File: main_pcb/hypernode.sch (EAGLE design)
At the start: 133 parts, among them IC1 74HCT245D, J1 AVR_SPI_PRG_62X3_LOCK, U1 MAX488, U2 PCA9685, U3 VOLTAGE_REGULATORDPACK, U4 ATMEGA328P, U5 MAX3421E, X1 USB-A-H, X10 JST-XH-03-PIN-LONG-PAD, X2 JST-XH-CONNECTOR-02-PIN, X4 JST-XH-CONNECTOR-02-PIN, X7 JST-XH-03-PIN-LONG-PAD, X8 JST-XH-03-PIN-LONG-PAD, X9 JST-XH-03-PIN-LONG-PAD, Y1 8MHZ

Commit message: remove unnecessary components from main pcb
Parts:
- removed C2, C3, C4, C6, C7: 100nF, Multischriever:CAPACITOR_0603
- removed C8: 1uF, Multischriever:CAPACITOR_0603
- removed C9: 4.7uF, Multischriever:CAPACITOR_0603
- removed D1, D3: (no value), Multischriever:DIODE_SOD-523
- removed HCPL0453: HCPL0700, optocoupler:HCPL0452
- removed J1: AVR_SPI_PRG_62X3_LOCK, SparkFun-Connectors:AVR_SPI_PRG_62X3_LOCK
- removed LED11, LED13, LED14, LED15, LED16, LED17, LED18, LED2, LED3, LED5, LED7, LED9: (no value), Multischriever:LED0603
- removed R12, R15, R18, R19, R22, R23, R26, R27, R3, R30, R31, R32, R33, R34, R35, R36, R37, R38, R39, R40, R41, R5: (no value), Multischriever:RESISTOR
- removed R13, R45, R46, R47: 180R, Multischriever:RESISTOR
- removed R14: 1K, Multischriever:RESISTOR
- removed R21, R24: 1k, Multischriever:RESISTOR
- removed R25, R28, R29, R42: 10k, Multischriever:RESISTOR
- removed R43, R44, R57: 4k7, Multischriever:RESISTOR
- removed R48, R50, R55, R56: 10K, Multischriever:RESISTOR
- removed R49, R9: 470R, Multischriever:RESISTOR
- removed R52: 100R, Multischriever:RESISTOR
- removed R53, R54, R6, R7: 33R, Multischriever:RESISTOR
- removed R8: 220R, Multischriever:RESISTOR
- removed REMOTE: M05X2NO_SILK, SparkFun-Connectors:M05X2NO_SILK
- removed U$1: ESP32POE, Multischriever:ESP32POE
- removed U$10, U$12, U$14, U$16, U$18, U$19, U$20, U$21, U$22, U$23, U$5, U$7: NCV8401_LOAD_SWITCH'DPAK+SOT23', Multischriever:NCV8401_LOAD_SWITCH'DPAK+SOT23'
- removed U$2, U$6: BIGTERMINAL, Multischriever:BIGTERMINAL
- removed U$24: 12MHz, adafruit:CERMOSCILL-AWCSR
- removed U$9: ESP8266_ESP12NOSILK, Multischriever:ESP8266_ESP12NOSILK
- removed U2: PCA9685, SparkFun-DigitalIC:PCA9685
- removed U3: VOLTAGE_REGULATORDPACK, Multischriever:VOLTAGE_REGULATORDPACK
- removed U4: ATMEGA328P, SparkFun-DigitalIC:ATMEGA328_SMT
- removed U5: MAX3421E, SparkFun-DigitalIC:MAX3421ESMD
- removed X1: USB-A-H, con-usb:USB-A-H
- removed X10, X9: JST-XH-03-PIN-LONG-PAD, Rembrandt Electronics - JST XH Connectors v1-0:JST-XH-03-PIN-LONG-PAD
- removed X11, X14, X16, X17, X19, X21, X22, X23, X24, X25, X26, X3: (no value), Multischriever:SCREW_TERMINAL_02-PINGREEN
- removed Y1: 8MHZ, SparkFun-FreqCtrl:RESONATOR8MHZ
- added U$17: WT32-ETH01, Multischriever:WT32-ETH01
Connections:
- removed net ENCA: R48.2, REMOTE.8, U$1.GPI34_BUT1
- removed net ENCBTN: R49.2, REMOTE.4, U$1.GPI39
- removed net MIDIIN: R50.2, R52.2, REMOTE.6, U$1.GPI35
- removed net N$1: R45.1, REMOTE.3
- removed net N$11: R45.2, U2.CH13
- removed net N$12: R46.1, REMOTE.5
- removed net N$14: R6.1, X10-1.S
- removed net N$15: R7.1, X10-3.S
- removed net N$17: D1.A, HCPL0453.C, X9-3.S
- removed net N$19: R5.1, U$7.G
- removed net N$20: R8.1, X9-1.S
- removed net N$21: D1.C, HCPL0453.A, R8.2
- removed net N$22: LED2.A, R3.1
- removed net N$23: R29.1, U$9.REST
- removed net N$24: LED2.C, U$7.D, X3-2.KL
- removed net N$27: R42.1, U$9.CH_PD
- removed net N$29: R21.2, U$9.TXD
- removed net N$30: R24.2, U$9.RXD
- removed net N$31: R28.2, U$9.GPIO0
- removed net N$32: R25.2, U$9.GPIO15
- removed net N$33: R47.1, REMOTE.7
- removed net N$35: R15.1, U$10.G
- removed net N$36: LED5.A, R12.1
- removed net N$37: LED5.C, U$10.D, X11-2.KL
- removed net N$39: HCPL0453.VO, R52.1, R9.2
- removed net N$40: U4.PB6(XTAL1/TOSC1), Y1.1
- removed net N$41: U4.PB7(XTAL2/TOSC2), Y1.3
- removed net N$42: U4.PD5(T1), U5.RES
- removed net N$43: R54.1, X1.D+
- removed net N$44: R53.1, X1.D-
- removed net N$45: LED3.C, U$5.D, X17-2.KL
- removed net N$46: R14.1, U$5.G
- removed net N$47: R19.1, U$12.G
- removed net N$48: LED7.A, R18.1
- removed net N$49: LED7.C, U$12.D, X14-2.KL
- removed net N$50: R53.2, U5.D-
- removed net N$51: R54.2, U5.D+
- removed net N$52: U$24.OUT, U5.X1
- removed net N$53: U$24.IN, U5.X0
- removed net N$54: U4.PD2(INT0), U5.INT
- removed net N$55: U4.PD3(INT1), U5.GPX
- removed net N$56: J1.4, U4.PB3(MOSI/OC2), U5.MOSI
- removed net N$57: J1.1, U4.PB4(MISO), U5.MISO
- removed net N$58: J1.3, U4.PB5(SCK), U5.SCK
- removed net N$59: R23.1, U$14.G
- removed net N$60: LED9.A, R22.1
- removed net N$61: LED9.C, U$14.D, X16-2.KL
- removed net N$62: LED3.A, R13.1
- removed net N$63: R56.1, U4.PB2(SS/OC1B), U5.SS
- removed net N$64: J1.5, R55.1, U4.PC6(/RESET)
- removed net N$68: D3.C, U4.PD1(TXD)
- removed net N$7: R47.2, U2.CH15
- removed net N$71: R27.1, U$16.G
- removed net N$72: LED11.A, R26.1
- removed net N$73: LED11.C, U$16.D, X19-2.KL
- removed net N$77: R31.1, U$18.G
- removed net N$78: LED13.A, R30.1
- removed net N$79: LED13.C, U$18.D, X21-2.KL
- removed net N$80: R33.1, U$19.G
- removed net N$81: LED14.A, R32.1
- removed net N$82: LED14.C, U$19.D, X22-2.KL
- removed net N$83: R35.1, U$20.G
- removed net N$84: LED15.A, R34.1
- removed net N$85: LED15.C, U$20.D, X23-2.KL
- removed net N$86: R37.1, U$21.G
- removed net N$87: LED16.A, R36.1
- removed net N$88: LED16.C, U$21.D, X24-2.KL
- removed net N$89: R39.1, U$22.G
- removed net N$9: R46.2, U2.CH14
- removed net N$90: LED17.A, R38.1
- removed net N$91: LED17.C, U$22.D, X25-2.KL
- removed net N$92: R41.1, U$23.G
- removed net N$93: LED18.A, R40.1
- removed net N$94: LED18.C, U$23.D, X26-2.KL
- removed net SCL: R44.1, REMOTE.10, U$1.GPIO16_I2C_SCL, U$9.GPIO5, U2.SCL, U4.PC5(ADC5/SCL)
- removed net SDA: R43.1, REMOTE.9, U$1.GPIO13_I2C_SDA, U$9.GPIO4, U2.SDA, U4.PC4(ADC4/SDA)
- removed net T1DRIVE1: R13.2, R14.2, U2.CH8
- removed net T1DRIVE10: R34.2, R35.2, U2.CH7
- removed net T1DRIVE11: R32.2, R33.2, U2.CH6
- removed net T1DRIVE12: R30.2, R31.2, U2.CH2
- removed net T1DRIVE2: R3.2, R5.2, U2.CH9
- removed net T1DRIVE3: R12.2, R15.2, U2.CH10
- removed net T1DRIVE4: R18.2, R19.2, U2.CH11
- removed net T1DRIVE5: R22.2, R23.2, U2.CH1
- removed net T1DRIVE6: R26.2, R27.2, U2.CH0
- removed net T1DRIVE7: R40.2, R41.2, U2.CH5
- removed net T1DRIVE8: R38.2, R39.2, U2.CH4
- removed net T1DRIVE9: R36.2, R37.2, U2.CH3
- removed net USBRX: D3.A, R57.2, U$1.GPIO3_U0RXD
- removed net USBTX: U$1.GPIO1_U0TXD, U4.PD0(RXD)
- new net DMXOUT: U$17.TXD, U1.DI
- net +3V3: now also U$17.3V3, U$17.3V3@1; no longer C2.1, C3.1, C4.1, C6.1, C7.1, C8.1, HCPL0453.VCC, J1.2, R28.1, R29.2, R42.2, R43.2, R44.2, R48.1, R50.1, R55.2, R56.2, R57.1, R6.2, R9.1, REMOTE.1, U$1.3V3, U$9.VCC, U2.VDD, U3.OUT, U4.AREF, U4.AVCC, U4.VCC@1, U4.VCC@2, U5.VCC, U5.VL
- net +5V: now also U$17.5V; no longer C9.1, U$1.5V, U3.IN, X1.VBUS
- net DMXIN: now also U$17.IO36; no longer R24.1, U$1.GPI36_U1RXD
- net GND: now also U$17.GND, U$17.GND@1, U$17.GND@2, U$17.GND@3, U$17.GND@4; no longer C2.2, C3.2, C4.2, C6.2, C7.2, C8.2, C9.2, HCPL0453.GND, J1.6, R25.1, R49.1, REMOTE.2, U$1.GND, U$10.S, U$12.S, U$14.S, U$16.S, U$18.S, U$19.S, U$2.P$1, U$20.S, U$21.S, U$22.S, U$23.S, U$24.GND, U$5.S, U$6.P$2, U$7.S, U$9.GND, U2.!OE, U2.A0, U2.A1, U2.A2, U2.A3, U2.A4, U2.A5, U2.EXTCLK, U2.VSS, U3.ADJ, U4.AGND, U4.GND@1, U4.GND@2, U5.GND@19, U5.GND@3, X1.GND, X10-2.S, Y1.2
- net VDD: no longer U$2.P$2, U$6.P$1, X11-1.KL, X14-1.KL, X16-1.KL, X17-1.KL, X19-1.KL, X21-1.KL, X22-1.KL, X23-1.KL, X24-1.KL, X25-1.KL, X26-1.KL, X3-1.KL
- net WS1: now also U$17.RXD; no longer R7.2, U$1.GPIO5_SPI_CS, U$9.GPIO16
- net WS2: now also U$17.IO4; no longer U$1.GPIO4_U1TXD, U$9.GPIO14
- net WS3: now also U$17.IO14; no longer U$1.GPIO14_HS2_CLK
- net WS4: now also U$17.IO2; no longer U$1.GPIO2_HS2_DATA0, U$9.GPIO12
- net WS5: now also U$17.IO15; no longer U$1.GPIO15_HS2_CMD
- net WS6: now also U$17.CFG; no longer R21.1, U$1.GPIO32, U1.DI
- net WS7: now also U$17.IO0; no longer U$1.GPIO0, U$9.GPIO13
- net WS8: now also U$17.485_EN; no longer U$1.GPIO33
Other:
- note removed: "BOOTPWM"
- note removed: "BOOTPWM, PU"
- note removed: "IN"
- note removed: "IN, BTN"
- note removed: "IN, DMX"
- note removed: "IN, MIDI"
- note removed: "SD"
- note removed: "SD, PD"
- note removed: "USBRX"
- note removed: "USBTX"
- note removed: "extra protection for if someone screws up the rotary encoder connections and connects 3v3 to this line"

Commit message: further cleanup and arrangement
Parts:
- removed R10: 100R, Multischriever:RESISTOR
- added C2: 100nF, Multischriever:CAPACITOR_0603
- added LED2: (no value), Multischriever:LED0603
- added PROGRAM: (no value), pinhead:PINHD-1X6
- added R3: 100R, Multischriever:RESISTOR
- added R5: 180R, Multischriever:RESISTOR
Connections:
- removed net N$10: IC1A.B6, R16.1
- removed net N$18: R20.2, U$11.6
- removed net N$25: R16.2, U$11.4
- removed net N$26: R10.2, U$11.2
- removed net N$28: R4.2, U$13.6
- removed net N$3: IC1A.B1, R1.1
- removed net N$5: IC1A.B2, R2.1
- removed net N$6: IC1A.B3, R4.1
- removed net N$8: IC1A.B5, R10.1
- removed net NIKS: IC1A.B4, R11.1
- removed net WS1-2: R1.2, U$13.2
- removed net WS2-2: R2.2, U$13.4
- removed net WS4-2: R11.2, U$13.8
- new net N$1: LED2.A, R5.1
- new net N$11: IC1A.B2, R20.1
- new net N$12: IC1A.B3, R16.1
- new net N$14: IC1A.B5, R11.1
- new net N$15: IC1A.B6, R4.1
- new net N$17: IC1A.B8, R1.1
- new net N$9: IC1A.B1, R17.1
- net +5V: now also C2.1
- net GND: now also C2.2, LED2.C
- net N$13: now also IC1A.B4, R3.1; no longer IC1A.B7, R20.1
- net N$16: now also IC1A.B7, R2.1; no longer IC1A.B8, R17.1
- net N$2: now also R5.2, U$17.IO12; no longer R17.2, U$11.8
- net WS1: now also IC1A.A4; no longer IC1A.A1
- net WS2: now also IC1A.A3; no longer IC1A.A2
- net WS3: now also IC1A.A2; no longer IC1A.A3
- net WS4: now also IC1A.A1; no longer IC1A.A4
- net WS5: now also IC1A.A8; no longer IC1A.A5
- net WS6: now also IC1A.A7; no longer IC1A.A6
- net WS7: now also IC1A.A6; no longer IC1A.A7
- net WS8: now also IC1A.A5; no longer IC1A.A8
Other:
- moved on the sheet: C5, IC1P, R1, R11, R16, R17, R2, R20, R4, U$11, U$13

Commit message: programmer
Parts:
- removed LED2: (no value), Multischriever:LED0603
- added LED_STATUS: (no value), Multischriever:LED0603
- added R7: 10K, Multischriever:RESISTOR
- U$17: value WT32-ETH01 -> WT32-ETH01WT32-ETH01-SMD; device Multischriever:WT32-ETH01 -> Multischriever:WT32-ETH01WT32-ETH01-SMD
- renumbered LED1 to LED_PWR
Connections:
- removed net N$2: R5.2, U$17.IO12
- new net EN: PROGRAM.4, U$17.EN, U$17.EN@1
- new net N$10: R2.2, U$13.4
- new net N$18: R4.2, U$13.6
- new net N$19: R11.2, U$13.8
- new net N$3: R3.2, U$11.2
- new net N$5: R16.2, U$11.4
- new net N$6: R20.2, U$11.6
- new net N$7: R17.2, U$11.8
- new net N$8: R1.2, U$13.2
- new net RX: PROGRAM.3, U$17.RX0
- new net TX: PROGRAM.2, U$17.TX0
- net +3V3: now also PROGRAM.1
- net DMXOUT: now also R5.1
- net GND: now also LED_STATUS.C, PROGRAM.6, R7.2; no longer LED2.C
- net N$1: now also LED_STATUS.A, R5.2; no longer LED2.A, R5.1
- net WS4: now also R7.1
- net WS7: now also PROGRAM.5, U$17.IO12; no longer U$17.IO0
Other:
- moved on the sheet: R5

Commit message: routing
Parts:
- removed U$8: POWERPOLE, Multischriever:POWERPOLE
- added R6: 180R, Multischriever:RESISTOR
- R5: value 180R -> 1K
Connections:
- new net N$2: LED_STATUS.A, R6.1
- new net N$20: U$17.3V3@1
- net +3V3: no longer U$17.3V3@1
- net DMXOUT: no longer R5.1
- net EN: no longer U$17.EN@1
- net GND: no longer U$8.P$2
- net N$1: now also PROGRAM.3, R5.1; no longer LED_STATUS.A, R5.2
- net RX: now also R5.2, R6.2; no longer PROGRAM.3
- net VDD: no longer U$8.P$1
- net WS1: now also U$17.IO14; no longer U$17.RXD
- net WS2: now also U$17.IO12; no longer U$17.IO4
- net WS3: now also U$17.IO4; no longer U$17.IO14
- net WS4: now also PROGRAM.5
- net WS6: now also U$17.RXD; no longer U$17.CFG
- net WS7: now also U$17.485_EN; no longer PROGRAM.5, U$17.IO12
- net WS8: now also U$17.CFG; no longer U$17.485_EN
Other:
- note added: "Do not use IO0. (RMII Clk)"
- moved on the sheet: LED_STATUS, R5

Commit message: rev A
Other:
- note added: "Input only"
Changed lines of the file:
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@@
 <plain>
 <text x="114.3" y="68.58" size="1.778" layer="91">Do not use IO0. (RMII Clk)</text>
+<text x="114.3" y="63.5" size="1.778" layer="91">Input only</text>
+<text x="114.3" y="50.8" size="1.778" layer="91">Input only</text>
 </plain>
 <instances>

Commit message: fix boot connetion
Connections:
- new net IO0: PROGRAM.5, U$17.IO0
- net WS4: no longer PROGRAM.5
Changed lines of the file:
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@@
 <description>MCU</description>
 <plain>
-<text x="114.3" y="68.58" size="1.778" layer="91">Do not use IO0. (RMII Clk)</text>
+<text x="127" y="68.58" size="1.778" layer="91">Do not use IO0.
+(RMII Clk)</text>
 <text x="114.3" y="63.5" size="1.778" layer="91">Input only</text>
 <text x="114.3" y="50.8" size="1.778" layer="91">Input only</text>
@@
 <label x="152.4" y="71.12" size="1.778" layer="95"/>
 </segment>
-<segment>
-<pinref part="PROGRAM" gate="A" pin="5"/>
-<wire x1="15.24" y1="-2.54" x2="-7.62" y2="-2.54" width="0.1524" layer="91"/>
-<label x="-7.62" y="-2.54" size="1.778" layer="95"/>
-</segment>
 </net>
 <net name="WS5" class="0">
@@
 </segment>
 </net>
+<net name="IO0" class="0">
+<segment>
+<pinref part="U$17" gate="G$1" pin="IO0"/>
+<wire x1="109.22" y1="68.58" x2="124.46" y2="68.58" width="0.1524" layer="91"/>
+<label x="121.92" y="68.58" size="1.778" layer="95"/>
+</segment>
+<segment>
+<pinref part="PROGRAM" gate="A" pin="5"/>
+<wire x1="15.24" y1="-2.54" x2="-7.62" y2="-2.54" width="0.1524" layer="91"/>
+<label x="-7.62" y="-2.54" size="1.778" layer="95"/>
+</segment>
+</net>
 </nets>
 </sheet>
@@
 </drawing>
 <compatibility>
+<note version="6.3" minversion="6.2.2" severity="warning">
+Since Version 6.2.2 text objects can contain more than one line,
+which will not be processed correctly with this version.
+</note>
 <note version="8.2" severity="warning">
 Since Version 8.2, EAGLE supports online libraries. The ids

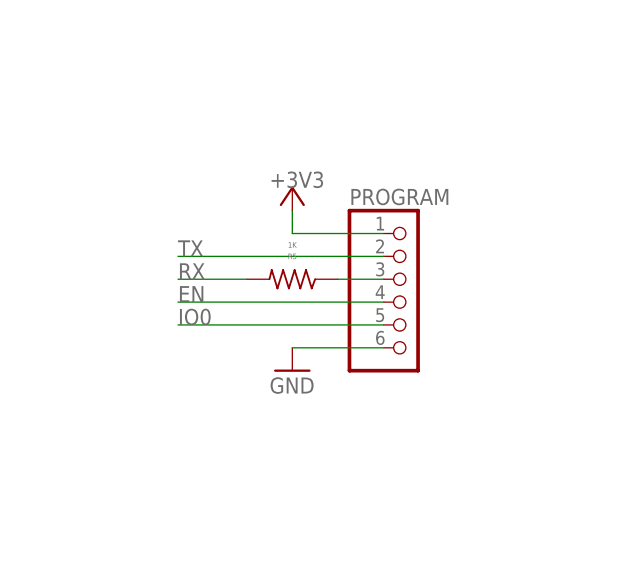
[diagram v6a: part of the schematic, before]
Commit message: change rx resistor to 2x100r
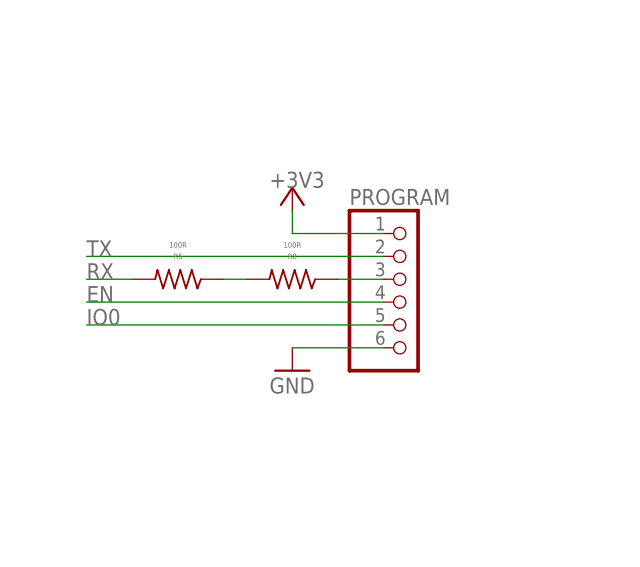
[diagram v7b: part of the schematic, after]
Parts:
- added R8: 100R, Multischriever:RESISTOR
- R5: value 1K -> 100R
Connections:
- new net N$21: PROGRAM.3, R8.1
- net N$1: now also R8.2; no longer PROGRAM.3
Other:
- moved on the sheet: R5
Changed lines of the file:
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@@
 <part name="LED_STATUS" library="Multischriever" deviceset="LED" device="0603"/>
 <part name="GND11" library="supply1" library_urn="urn:adsk.eagle:library:371" deviceset="GND" device=""/>
-<part name="R5" library="Multischriever" deviceset="RESISTOR" device="" value="1K"/>
+<part name="R5" library="Multischriever" deviceset="RESISTOR" device="" value="100R"/>
+<part name="R8" library="Multischriever" deviceset="RESISTOR" device="" value="100R"/>
 </parts>
 <sheets>
@@
 <attribute name="VALUE" x="134.62" y="86.36" size="1.778" layer="96"/>
 </instance>
-<instance part="R5" gate="G$1" x="5.08" y="2.54" smashed="yes" rot="R180">
+<instance part="R5" gate="G$1" x="-7.62" y="2.54" smashed="yes" rot="R180">
+<attribute name="NAME" x="-7.62" y="5.08" size="0.6096" layer="95" rot="R180" align="center"/>
+<attribute name="VALUE" x="-7.62" y="6.35" size="0.6096" layer="96" rot="R180" align="center"/>
+</instance>
+<instance part="R8" gate="G$1" x="5.08" y="2.54" smashed="yes" rot="R180">
 <attribute name="NAME" x="5.08" y="5.08" size="0.6096" layer="95" rot="R180" align="center"/>
 <attribute name="VALUE" x="5.08" y="6.35" size="0.6096" layer="96" rot="R180" align="center"/>
@@
 <segment>
 <pinref part="PROGRAM" gate="A" pin="2"/>
-<wire x1="15.24" y1="5.08" x2="-7.62" y2="5.08" width="0.1524" layer="91"/>
-<label x="-7.62" y="5.08" size="1.778" layer="95"/>
+<wire x1="15.24" y1="5.08" x2="-17.78" y2="5.08" width="0.1524" layer="91"/>
+<label x="-17.78" y="5.08" size="1.778" layer="95"/>
 </segment>
 </net>
@@
 </segment>
 <segment>
-<label x="-7.62" y="2.54" size="1.778" layer="95"/>
+<label x="-17.78" y="2.54" size="1.778" layer="95"/>
 <pinref part="R5" gate="G$1" pin="2"/>
-<wire x1="0" y1="2.54" x2="-7.62" y2="2.54" width="0.1524" layer="91"/>
+<wire x1="-12.7" y1="2.54" x2="-17.78" y2="2.54" width="0.1524" layer="91"/>
 </segment>
 </net>
@@
 <segment>
 <pinref part="PROGRAM" gate="A" pin="4"/>
-<wire x1="15.24" y1="0" x2="-7.62" y2="0" width="0.1524" layer="91"/>
-<label x="-7.62" y="0" size="1.778" layer="95"/>
+<wire x1="15.24" y1="0" x2="-17.78" y2="0" width="0.1524" layer="91"/>
+<label x="-17.78" y="0" size="1.778" layer="95"/>
 </segment>
 </net>
@@
 </segment>
 </net>
-<net name="N$1" class="0">
-<segment>
-<pinref part="R5" gate="G$1" pin="1"/>
-<pinref part="PROGRAM" gate="A" pin="3"/>
-<wire x1="10.16" y1="2.54" x2="15.24" y2="2.54" width="0.1524" layer="91"/>
-</segment>
-</net>
 <net name="N$20" class="0">
 <segment>
@@
 <segment>
 <pinref part="PROGRAM" gate="A" pin="5"/>
-<wire x1="15.24" y1="-2.54" x2="-7.62" y2="-2.54" width="0.1524" layer="91"/>
-<label x="-7.62" y="-2.54" size="1.778" layer="95"/>
-</segment>
-</net>
+<wire x1="15.24" y1="-2.54" x2="-17.78" y2="-2.54" width="0.1524" layer="91"/>
+<label x="-17.78" y="-2.54" size="1.778" layer="95"/>
+</segment>
+</net>
+<net name="N$1" class="0">
+<segment>
+<pinref part="R5" gate="G$1" pin="1"/>
+<pinref part="R8" gate="G$1" pin="2"/>
+<wire x1="-2.54" y1="2.54" x2="0" y2="2.54" width="0.1524" layer="91"/>
+</segment>
+</net>
+<net name="N$21" class="0">
+<segment>
+<pinref part="R8" gate="G$1" pin="1"/>
+<pinref part="PROGRAM" gate="A" pin="3"/>
+<wire x1="10.16" y1="2.54" x2="15.24" y2="2.54" width="0.1524" layer="91"/>
+</segment>
+</net>

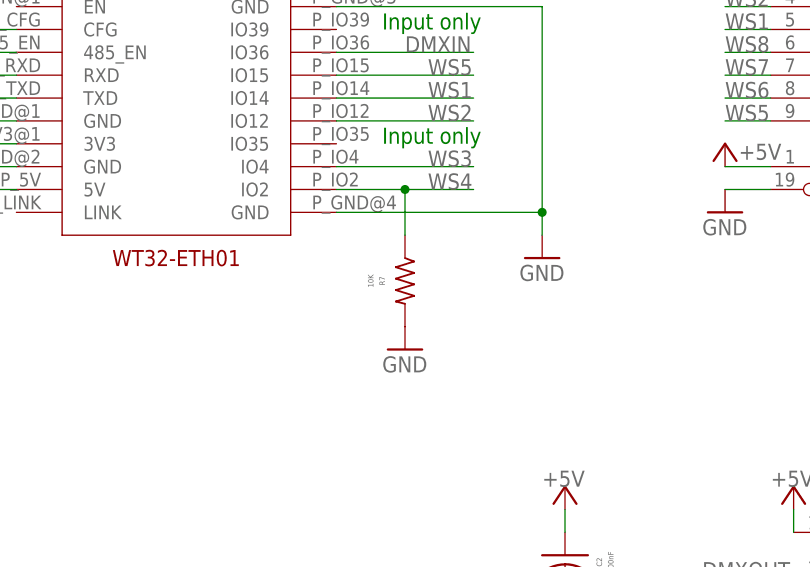
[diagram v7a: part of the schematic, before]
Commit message: remove unnecessary pull down resistor
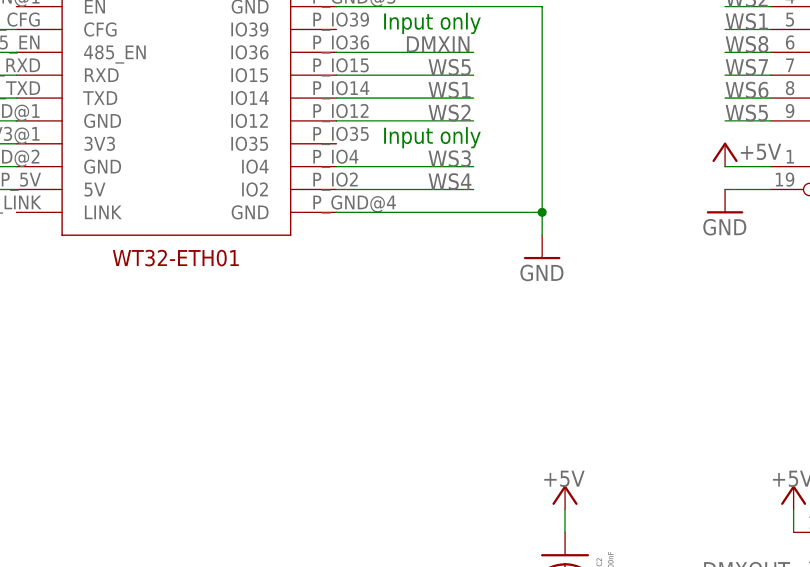
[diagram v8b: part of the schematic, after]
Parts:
- removed R7: 10K, Multischriever:RESISTOR
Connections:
- net GND: no longer R7.2
- net WS4: no longer R7.1
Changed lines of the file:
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@@
 <part name="GND9" library="supply1" library_urn="urn:adsk.eagle:library:371" deviceset="GND" device=""/>
 <part name="+3V3" library="supply1" library_urn="urn:adsk.eagle:library:371" deviceset="+3V3" device=""/>
-<part name="R7" library="Multischriever" deviceset="RESISTOR" device="" value="10K"/>
-<part name="GND10" library="supply1" library_urn="urn:adsk.eagle:library:371" deviceset="GND" device=""/>
 <part name="R6" library="Multischriever" deviceset="RESISTOR" device="" value="180R"/>
 <part name="LED_STATUS" library="Multischriever" deviceset="LED" device="0603"/>
@@
 <instance part="+3V3" gate="G$1" x="5.08" y="12.7" smashed="yes">
 <attribute name="VALUE" x="2.54" y="12.7" size="1.778" layer="96"/>
-</instance>
-<instance part="R7" gate="G$1" x="116.84" y="35.56" smashed="yes" rot="R270">
-<attribute name="NAME" x="114.3" y="35.56" size="0.6096" layer="95" rot="R270" align="center"/>
-<attribute name="VALUE" x="113.03" y="35.56" size="0.6096" layer="96" rot="R270" align="center"/>
-</instance>
-<instance part="GND10" gate="1" x="116.84" y="27.94" smashed="yes">
-<attribute name="VALUE" x="114.3" y="25.4" size="1.778" layer="96"/>
 </instance>
 <instance part="R6" gate="G$1" x="121.92" y="93.98" smashed="yes" rot="R180">
@@
 </segment>
 <segment>
-<pinref part="R7" gate="G$1" pin="2"/>
-<pinref part="GND10" gate="1" pin="GND"/>
-</segment>
-<segment>
 <pinref part="LED_STATUS" gate="G$1" pin="C"/>
 <pinref part="GND11" gate="1" pin="GND"/>
@@
 <segment>
 <pinref part="U$17" gate="G$1" pin="IO2"/>
-<wire x1="109.22" y1="45.72" x2="116.84" y2="45.72" width="0.1524" layer="91"/>
 <label x="119.38" y="45.72" size="1.778" layer="95"/>
-<pinref part="R7" gate="G$1" pin="1"/>
-<wire x1="116.84" y1="45.72" x2="124.46" y2="45.72" width="0.1524" layer="91"/>
-<wire x1="116.84" y1="40.64" x2="116.84" y2="45.72" width="0.1524" layer="91"/>
-<junction x="116.84" y="45.72"/>
-</segment>
-<segment>
+<wire x1="109.22" y1="45.72" x2="124.46" y2="45.72" width="0.1524" layer="91"/>
+</segment>
+<segment>
